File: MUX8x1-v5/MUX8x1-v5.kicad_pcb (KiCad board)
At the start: 4 copper layers, 99.1 x 99.1 mm, 49 parts, among them J1 Conn_01x09_Male, J10 Conn_01x03_Male, J11 Conn_01x09_Male, J12 Conn_01x09_Male, J14 Conn_01x09_Male, J15 Conn_01x09_Male, J16 Conn_01x09_Male, J18 Conn_01x09_Male, J2 Conn_01x09_Male, J20 Conn_01x01_Male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

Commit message: MUX8:1 v5. Routing.
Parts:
- moved C1 2.54 mm to (66.0, 59.7)
- moved C2 2.54 mm to (83.8, 59.7)
- moved C3 2.54 mm to (101.6, 59.7)
- moved C4 2.54 mm to (119.4, 59.7)
- moved U1 2.54 mm to (62.2, 58.4)
- moved U2 2.54 mm to (80.0, 58.4)
- moved U3 2.54 mm to (97.8, 58.4)
- moved U4 2.54 mm to (115.6, 58.4)
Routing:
- net /S1: track 0.00 -> 213.7 mm
- net /E3: track 0.00 -> 206.6 mm
- net /~E: track 0.00 -> 200.9 mm
- net /S0: track 0.00 -> 197.3 mm
- net /S2: track 0.00 -> 183.5 mm
- net /B5: track 0.00 -> 156.4 mm
- net /G3: track 0.00 -> 151.2 mm, vias 0 -> 1
- net /D4: track 0.00 -> 125.7 mm
- net /B4: track 0.00 -> 117.5 mm
- net /B6: track 0.00 -> 100.2 mm
- net /G2: track 0.00 -> 99.7 mm
- net /H0: track 0.00 -> 98.4 mm, vias 0 -> 1
- net /F0: track 0.00 -> 97.2 mm, vias 0 -> 1
- net /D5: track 0.00 -> 94.4 mm
- net /O0: track 0.00 -> 86.8 mm, vias 0 -> 1
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
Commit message: MUX8:1 v5. Routing.
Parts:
- moved C9 0.64 mm to (137.2, 78.1)
- moved C4 0.63 mm to (119.4, 59.1)
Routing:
- net /E3: track 206.6 -> 133.3 mm, vias 0 -> 1
- net VCC: track 14.1 -> 4.71 mm
- net /E0: track 76.3 -> 68.5 mm
- net /H4: track 85.3 -> 92.5 mm
- net /G3: track 151.2 -> 157.0 mm
- net /G6: track 46.1 -> 51.8 mm
- net /O7: track 21.5 -> 26.5 mm
- net /A5: track 60.0 -> 64.9 mm
- net /H5: track 65.1 -> 69.9 mm
- net /O0: track 86.8 -> 91.3 mm
- net GND: track 21.2 -> 16.8 mm
- net /S1: track 213.7 -> 218.1 mm
- net /O1: track 66.5 -> 70.7 mm
- net /E4: track 39.6 -> 43.6 mm
- net /H0: track 98.4 -> 102.4 mm
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
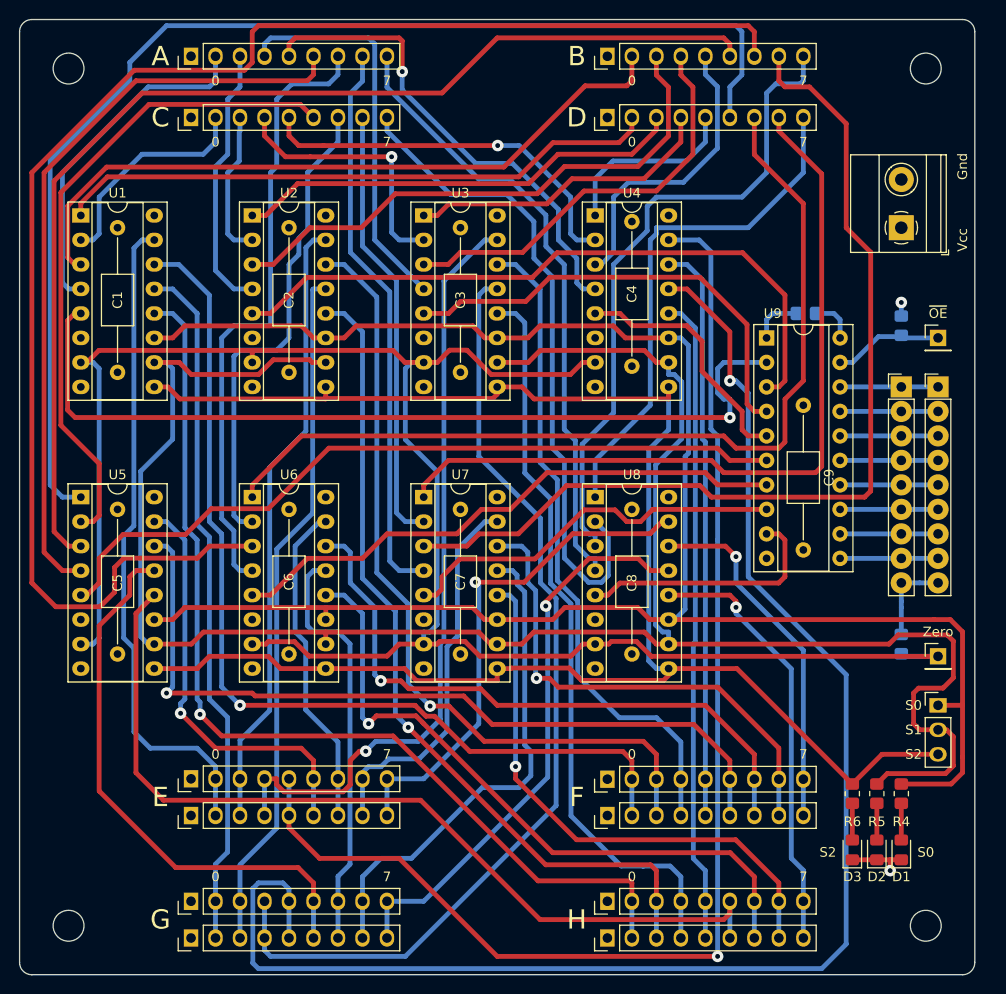
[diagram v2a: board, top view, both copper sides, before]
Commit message: Polishing MUX8:1
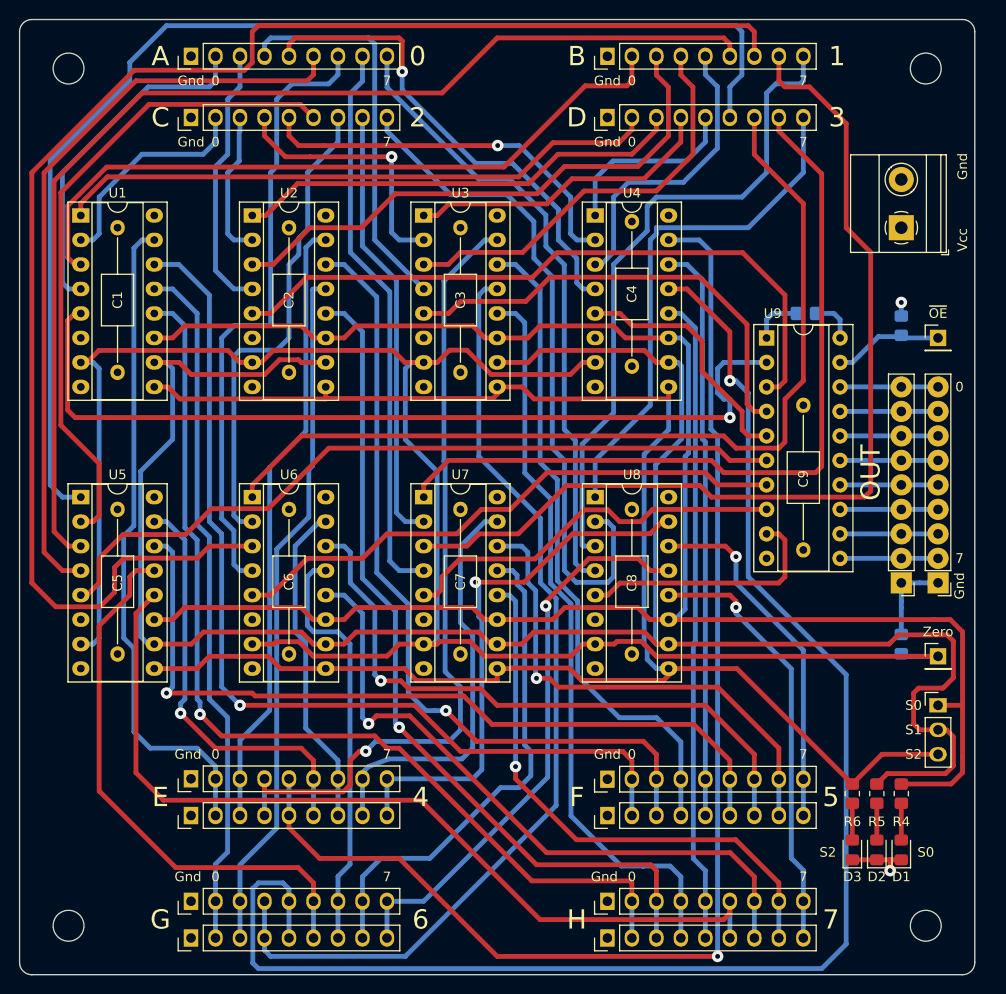
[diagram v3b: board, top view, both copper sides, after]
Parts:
- moved J21 20.3 mm to (151.1, 96.5), turned to 180 degrees
- moved J3 20.3 mm to (147.3, 96.5), turned to 180 degrees
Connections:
- J21 pad 1: /BUS0 -> GND
- J21 pad 2: /BUS1 -> /BUS7
- J21 pad 3: /BUS2 -> /BUS6
- J21 pad 4: /BUS3 -> /BUS5
- J21 pad 6: /BUS5 -> /BUS3
- J21 pad 7: /BUS6 -> /BUS2
- J21 pad 8: /BUS7 -> /BUS1
- J21 pad 9: GND -> /BUS0
- J3 pad 1: /BUS0 -> GND
- J3 pad 2: /BUS1 -> /BUS7
- J3 pad 3: /BUS2 -> /BUS6
- J3 pad 4: /BUS3 -> /BUS5
- J3 pad 6: /BUS5 -> /BUS3
- J3 pad 7: /BUS6 -> /BUS2
- J3 pad 8: /BUS7 -> /BUS1
- J3 pad 9: GND -> /BUS0
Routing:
- net /E2: track 80.4 -> 84.1 mm
- net /E6: track 39.6 -> 43.1 mm
- net /E7: track 53.2 -> 56.4 mm
- net /C7: track 68.8 -> 71.1 mm
- net /H1: track 86.5 -> 87.0 mm
- net /F1: track 83.3 -> 83.8 mm
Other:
- board text added: "1"
- board text added: "2"
- board text added: "3"
- board text added: "4"
- board text added: "5"
- board text added: "6"
- board text added: "OUT"

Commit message: MUX8:1, lost labels
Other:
- board text added: "18.02.2023"
- board text added: "74HCPU"
- board text added: "MUX8:1"
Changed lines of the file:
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@@
   (general
     (thickness 1.6)
-    (drawings 61)
+    (drawings 64)
     (tracks 1010)
     (zones 0)
@@
     (pad 1 np_thru_hole circle (at 0 0) (size 3.2 3.2) (drill 3.2) (layers *.Cu *.Mask))
   )
+  (gr_text 18.02.2023 (at 62.23 119.38 90) (layer F.Cu)
+    (effects (font (size 1.5 1.5) (thickness 0.3)))
+  )
+  (gr_text 74HCPU (at 59.055 121.285 90) (layer F.Cu)
+    (effects (font (size 1.5 1.5) (thickness 0.3)))
+  )
+  (gr_text MUX8:1 (at 105.41 82.55) (layer F.SilkS)
+    (effects (font (size 3 3) (thickness 0.5)))
+  )
   (gr_text OUT (at 144.145 85.09 90) (layer F.SilkS)

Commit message: Fix some silk
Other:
- board text added: "+5V"
- board text added: "151"
- board text added: "245"

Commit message: MUX8:1 - Now it have 2 zero line
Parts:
- added J13: Conn_01x01_Male, Connector_PinHeader_2.54mm:PinHeader_1x01_P2.54mm_Vertical, F.Cu at (151.1, 64.8)
- added R7: 10k, Resistor_SMD:R_0805_2012Metric_Pad1.20x1.40mm_HandSolder, B.Cu at (147.3, 65.0)
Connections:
- J20 pad 1: /~E -> /~EH
- R1 pad 1: /~E -> /~EH
- U1 pad 7: /~E -> /~EL
- U2 pad 7: /~E -> /~EL
- U3 pad 7: /~E -> /~EL
- U4 pad 7: /~E -> /~EL
- U5 pad 7: /~E -> /~EH
- U6 pad 7: /~E -> /~EH
- U7 pad 7: /~E -> /~EH
- U8 pad 7: /~E -> /~EH
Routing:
- net /~E: track 201.3 -> 0.00 mm
- net /~EL: track 0.00 -> 98.1 mm, vias 0 -> 1
- net /~EH: track 0.00 -> 98.0 mm
- net /O3: track 26.0 -> 37.6 mm
- net /G3: track 157.0 -> 166.4 mm
- net /O2: track 47.7 -> 56.4 mm
- net /G4: track 58.2 -> 64.3 mm
- net /O1: track 70.7 -> 73.5 mm
- net /S1: track 218.5 -> 221.1 mm
- net /E0: track 68.5 -> 71.1 mm
- net GND: track 16.8 -> 18.2 mm
- net /B3: track 31.1 -> 31.8 mm
- net /S2: track 182.0 -> 181.2 mm
- net /H4: track 92.5 -> 91.8 mm, vias 0 -> 1
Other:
- board text added: "29.07.2023"
- board text added: "ZeroH"
- board text added: "ZeroL"
- board text removed: "+5V"
- board text removed: "18.02.2023"
- board text removed: "Zero"
